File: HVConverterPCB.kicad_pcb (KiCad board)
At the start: 2 copper layers, 70 x 50 mm, 9 parts, among them J3 VOUT, J4 JST_CONN_VIN, J5 JST_CONN_DAC, J6 Conn_01x03, J7 MCP4725_DUPONT_CONN

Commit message: Removed Via Stitching, Copper Pours
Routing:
- net (no net): vias 222 -> 0
- removed copper zone on F.Cu, net (none)
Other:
- board text removed: "ESP32"

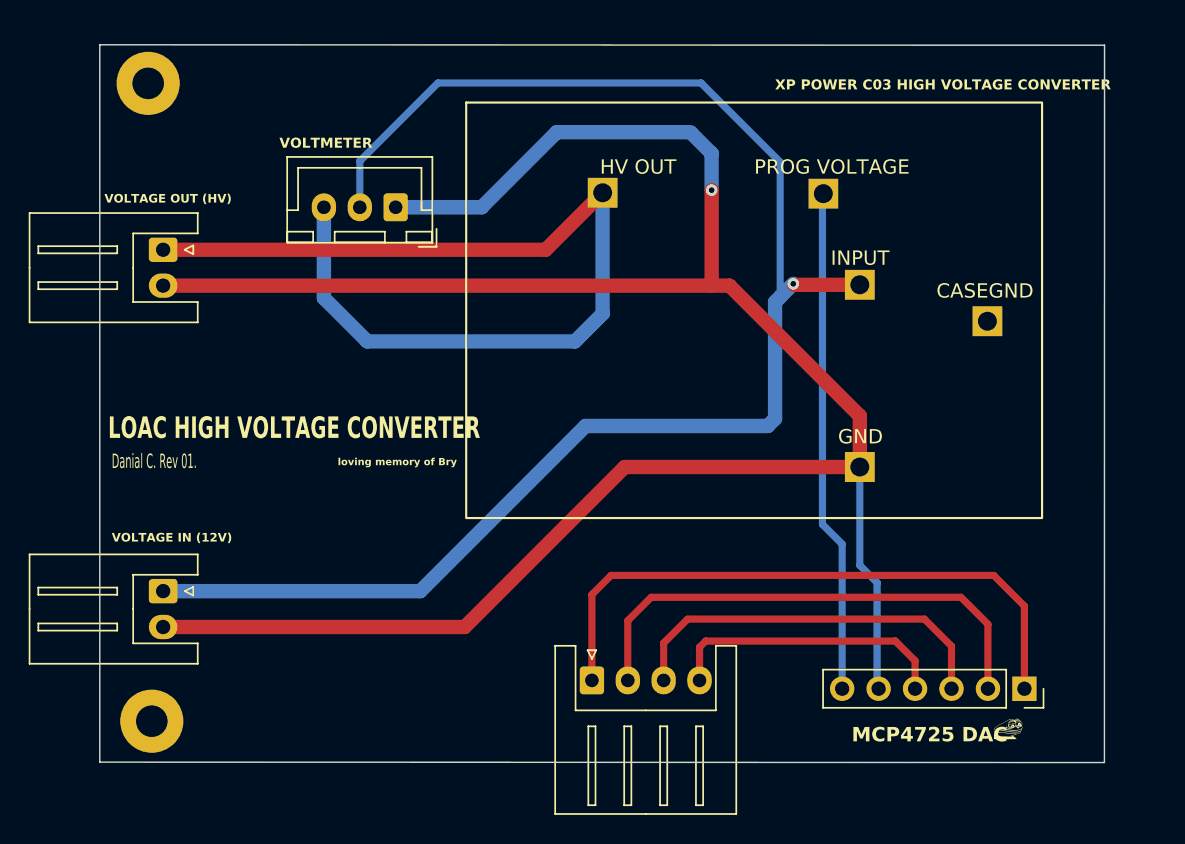
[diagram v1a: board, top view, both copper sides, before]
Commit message: Added more silkscreens
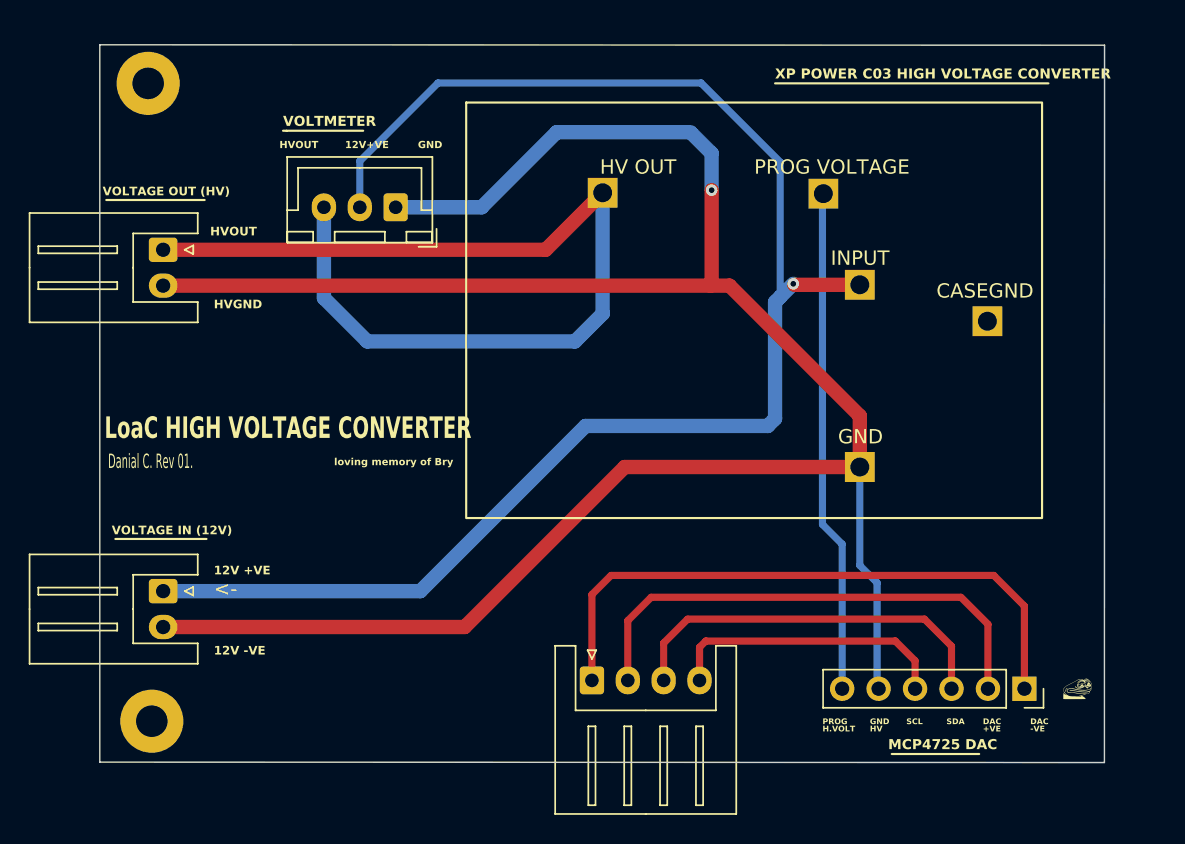
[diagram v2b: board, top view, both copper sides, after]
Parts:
- moved G*** 5.58 mm to (192.8, 112.3)
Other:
- board text added: "+VE"
- board text added: "-VE"
- board text added: "12V +VE"
- board text added: "12V -VE"
- board text added: "12V+VE"
- board text added: "<-"
- board text added: "DAC"
- board text added: "GND"
- board text added: "H.VOLT"
- board text added: "HV"
- board text added: "HVGND"
- board text added: "HVOUT"
- board text added: "LoaC HIGH VOLTAGE CONVERTER"
- board text added: "PROG"
- board text added: "SCL"
- board text added: "SDA"
- board text removed: "LOAC HIGH VOLTAGE CONVERTER"
